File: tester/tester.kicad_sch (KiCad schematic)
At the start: 70 parts

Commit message: reorg
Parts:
- renumbered D18 to D11, D26 to D12, D37 to D13, D38 to D14, D39 to D15, D40 to D16, D3 to D17, D11 to D18, D9 to D2, D27 to D20, D41 to D21, D42 to D22, D43 to D23, D44 to D24, D4 to D25, D12 to D26, D20 to D27, D45 to D29, D17 to D3, D46 to D30, D47 to D31, D48 to D32, D5 to D33, D13 to D34, D21 to D35, D29 to D36, D49 to D37, D50 to D38, D51 to D39, D25 to D4, D52 to D40, D6 to D41, D14 to D42, D22 to D43, D30 to D44, D53 to D45, D54 to D46, D55 to D47, D56 to D48, D7 to D49, D33 to D5, D15 to D50, D23 to D51, D31 to D52, D57 to D53, D58 to D54, D59 to D55, D60 to D56, D8 to D57, D16 to D58, D24 to D59, D34 to D6, D32 to D60, D35 to D7, D36 to D8, D2 to D9

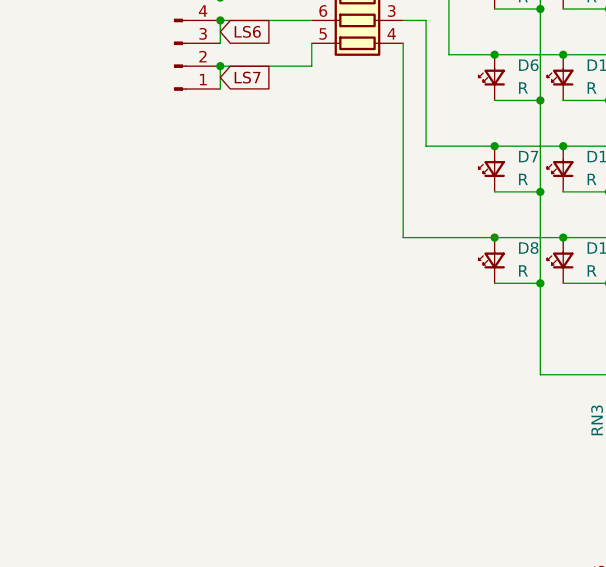
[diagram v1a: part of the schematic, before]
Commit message: led tester
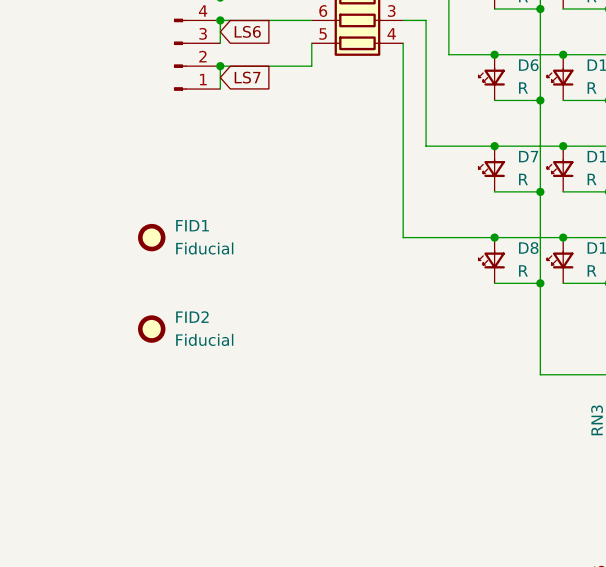
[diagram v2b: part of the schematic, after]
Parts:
- added FID1: Fiducial, Fiducial:Fiducial_Cross_1.5mm_Mask2mm, symbol Mechanical:Fiducial
- added FID2: Fiducial, Fiducial:Fiducial_0.5mm_Mask1.5mm, symbol Mechanical:Fiducial
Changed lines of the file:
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@@
+	)
+	(symbol
+		(lib_id "Mechanical:Fiducial")
+		(at 30.48 99.06 0)
+		(unit 1)
+		(exclude_from_sim no)
+		(in_bom no)
+		(on_board yes)
+		(dnp no)
+		(fields_autoplaced yes)
+		(property "Reference" "FID2"
+			(at 33.02 97.7899 0)
+			(effects
+				(font
+					(size 1.27 1.27)
+				)
+				(justify left)
+			)
+		)
+		(property "Value" "Fiducial"
+			(at 33.02 100.3299 0)
+			(effects
+				(font
+					(size 1.27 1.27)
+				)
+				(justify left)
+			)
+		)
+		(property "Footprint" "Fiducial:Fiducial_0.5mm_Mask1.5mm"
+			(at 30.48 99.06 0)
+			(effects
+				(font
+					(size 1.27 1.27)
+				)
+				(hide yes)
+			)
+		)
+		(property "Datasheet" "~"
+			(at 30.48 99.06 0)
+			(effects
+				(font
+					(size 1.27 1.27)
+				)
+				(hide yes)
+			)
+		)
+		(property "Description" "Fiducial Marker"
+			(at 30.48 99.06 0)
+			(effects
+				(font
+					(size 1.27 1.27)
+				)
+				(hide yes)
+			)
+		)
+		(instances
+			(project "tester"
+				(path "/c758d11b-85df-45f2-b623-a0eb46e04509"
+					(reference "FID2")
+					(unit 1)
+				)
+			)
+		)
 	)
 	(symbol
@@
 					(unit 1)
 				)
+			)
+		)
+	)
+	(symbol
+		(lib_id "Mechanical:Fiducial")
+		(at 30.48 88.9 0)
+		(unit 1)
+		(exclude_from_sim no)
+		(in_bom no)
+		(on_board yes)
+		(dnp no)
+		(fields_autoplaced yes)
+		(property "Reference" "FID1"
+			(at 33.02 87.6299 0)
+			(effects
+				(font
+					(size 1.27 1.27)
+				)
+				(justify left)
+			)
+		)
+		(property "Value" "Fiducial"
+			(at 33.02 90.1699 0)
+			(effects
+				(font
+					(size 1.27 1.27)
+				)
+				(justify left)
+			)
+		)
+		(property "Footprint" "Fiducial:Fiducial_Cross_1.5mm_Mask2mm"
+			(at 30.48 88.9 0)
+			(effects
+				(font
+					(size 1.27 1.27)
+				)
+				(hide yes)
+			)
+		)
+		(property "Datasheet" "~"
+			(at 30.48 88.9 0)
+			(effects
+				(font
+					(size 1.27 1.27)
+				)
+				(hide yes)
+			)
+		)
+		(property "Description" "Fiducial Marker"
+			(at 30.48 88.9 0)
+			(effects
+				(font
+					(size 1.27 1.27)
+				)
+				(hide yes)
+			)
+		)
+		(instances
+			(project ""
+				(path "/c758d11b-85df-45f2-b623-a0eb46e04509"
+					(reference "FID1")
+					(unit 1)
+				)

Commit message: name
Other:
- company: (none) -> stonedDiscord
- title: (none) -> Matrixtester
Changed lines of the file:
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@@
 	(generator_version "9.0")
 	(paper "A4")
+	(title_block
+		(title "Matrixtester")
+		(company "stonedDiscord")
+	)
 	(junction
 		(at 106.68 17.78)
